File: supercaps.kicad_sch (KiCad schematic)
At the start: 17 parts, among them J8 XT30_F, J9 XT30_F, Q10 2SAR587D3, Q9 2SCR587D3, U17 TLV9301xDBV

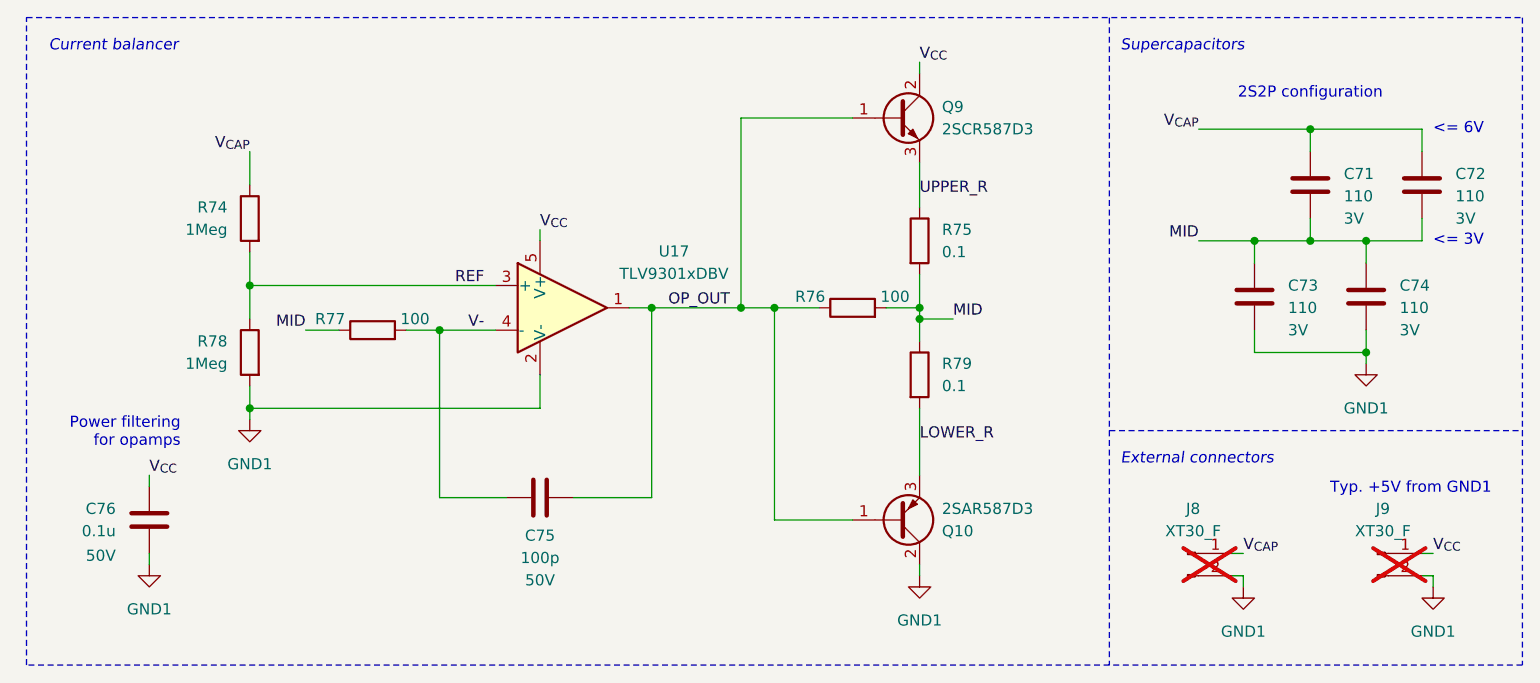
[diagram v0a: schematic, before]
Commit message: Add test points to all subsheets
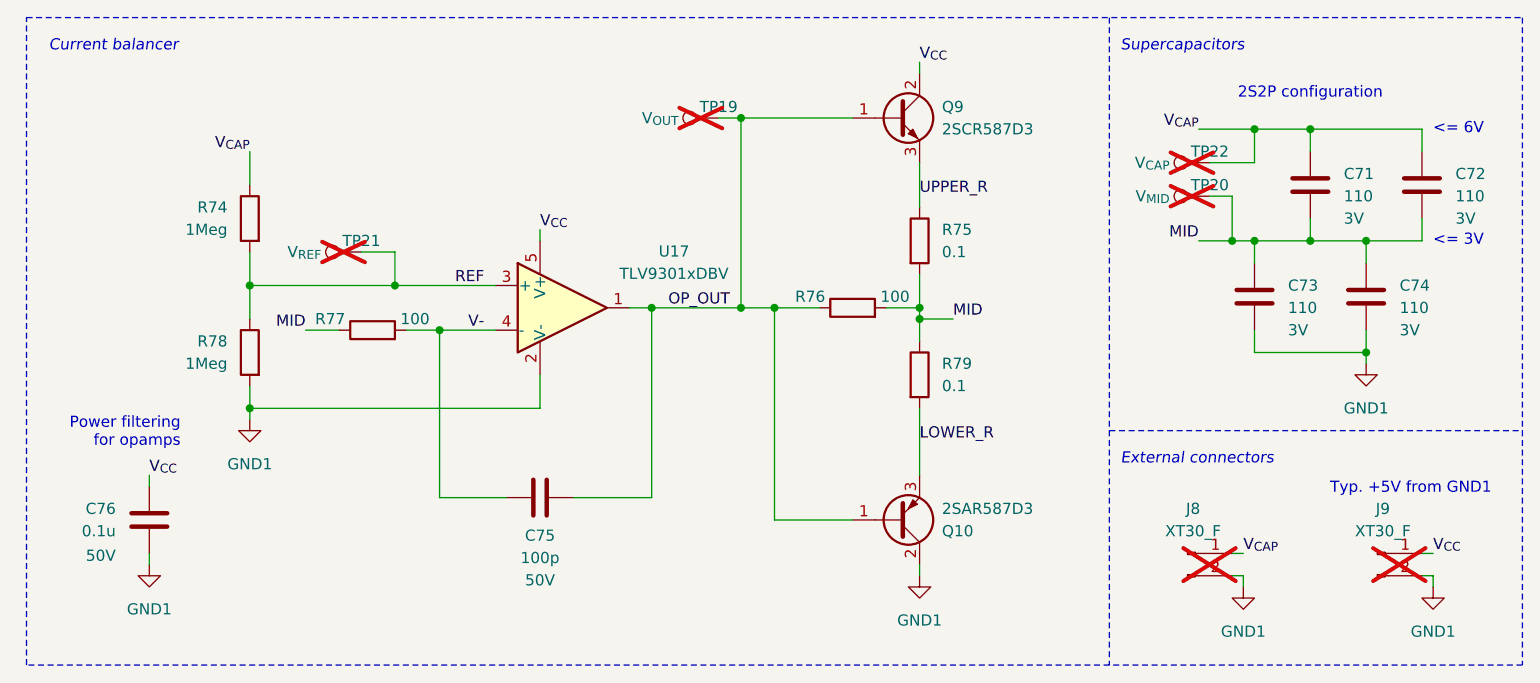
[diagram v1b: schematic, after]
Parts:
- added TP19: V_{OUT}, TestPoint:TestPoint_Bridge_Pitch2.0mm_Drill0.7mm, symbol Connector:TestPoint
- added TP20: V_{MID}, TestPoint:TestPoint_Bridge_Pitch2.0mm_Drill0.7mm, symbol Connector:TestPoint
- added TP21: V_{REF}, TestPoint:TestPoint_Bridge_Pitch2.0mm_Drill0.7mm, symbol Connector:TestPoint
- added TP22: V_{CAP}, TestPoint:TestPoint_Bridge_Pitch2.0mm_Drill0.7mm, symbol Connector:TestPoint
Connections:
- net MID: now also TP20.1
- net OP_OUT: now also TP19.1
- net REF: now also TP21.1
- net V_{CAP}: now also TP22.1

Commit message: Renumbered components for rev 1b layout
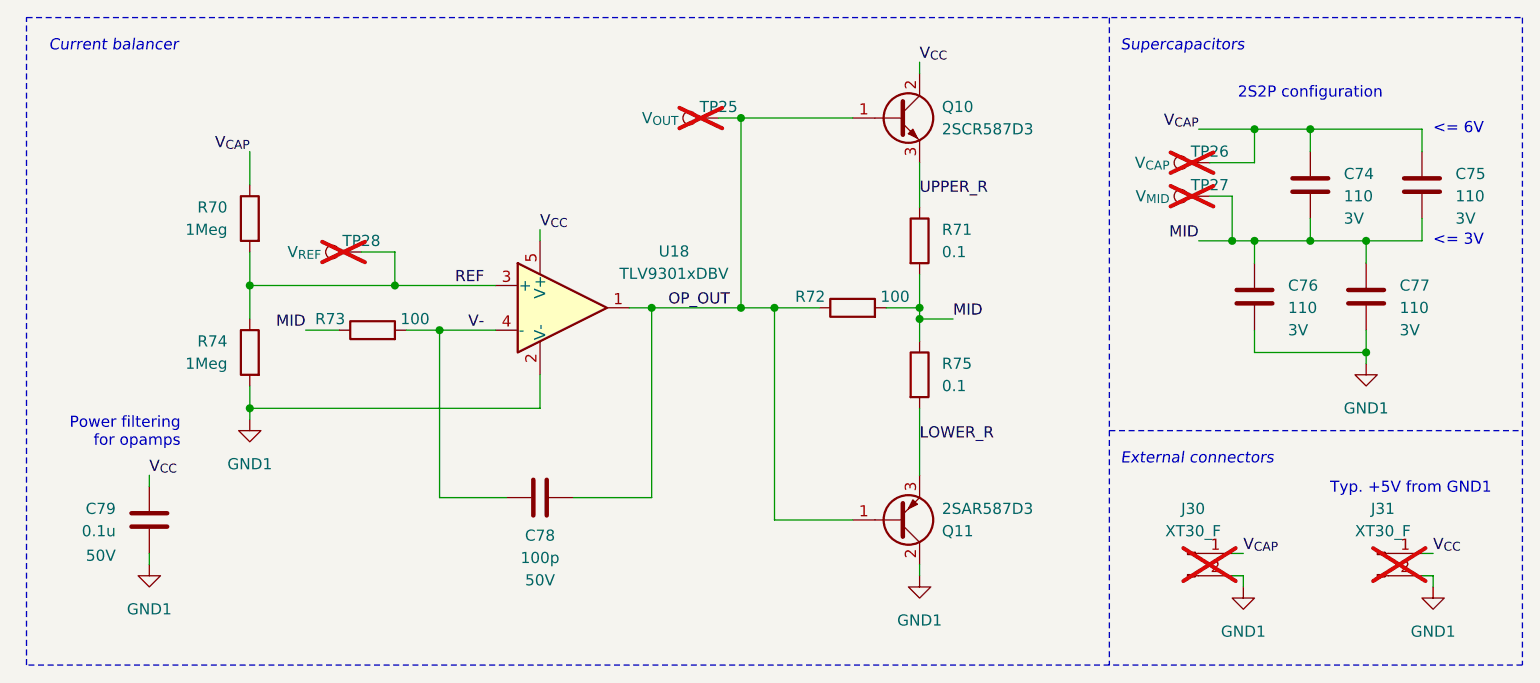
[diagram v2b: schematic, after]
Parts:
- renumbered C71 to C74, C72 to C75, C73 to C76, C74 to C77, C75 to C78, C76 to C79, J8 to J30, J9 to J31, Q9 to Q10, Q10 to Q11, R74 to R70, R75 to R71, R76 to R72, R77 to R73, R78 to R74, R79 to R75, TP19 to TP25, TP22 to TP26, TP20 to TP27, TP21 to TP28, U17 to U18
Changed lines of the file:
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@@
 		(on_board yes)
 		(dnp yes)
-		(property "Reference" "TP21"
+		(property "Reference" "TP28"
 			(at 59.69 50.8 90)
 			(effects
@@
 			(project "Rev 1B"
 				(path "/e5f99deb-ef42-4c5f-b80a-388477910e20/1165d5b5-e274-4083-890a-7a12aee56ddf"
-					(reference "TP21")
+					(reference "TP28")
 					(unit 1)
 				)
@@
 		(on_board yes)
 		(dnp no)
-		(property "Reference" "R?"
+		(property "Reference" "R75"
 			(at 125.73 64.7699 0)
 			(effects
@@
 			(project "Rev 1B"
 				(path "/e5f99deb-ef42-4c5f-b80a-388477910e20/1165d5b5-e274-4083-890a-7a12aee56ddf"
-					(reference "R?")
+					(reference "R75")
 					(unit 1)
 				)
@@
 		(on_board yes)
 		(dnp no)
-		(property "Reference" "U?"
+		(property "Reference" "U18"
 			(at 95.25 51.9998 0)
 			(effects
@@
 			(project "Rev 1B"
 				(path "/e5f99deb-ef42-4c5f-b80a-388477910e20/1165d5b5-e274-4083-890a-7a12aee56ddf"
-					(reference "U?")
+					(reference "U18")
 					(unit 1)
 				)
@@
 		(on_board yes)
 		(dnp yes)
-		(property "Reference" "TP19"
+		(property "Reference" "TP25"
 			(at 100.33 35.56 90)
 			(effects
@@
 			(project "Rev 1B"
 				(path "/e5f99deb-ef42-4c5f-b80a-388477910e20/1165d5b5-e274-4083-890a-7a12aee56ddf"
-					(reference "TP19")
+					(reference "TP25")
 					(unit 1)
 				)
@@
 		(on_board yes)
 		(dnp no)
-		(property "Reference" "C?"
+		(property "Reference" "C78"
 			(at 80.01 84.328 90)
 			(effects
@@
 			(project "Rev 1B"
 				(path "/e5f99deb-ef42-4c5f-b80a-388477910e20/1165d5b5-e274-4083-890a-7a12aee56ddf"
-					(reference "C?")
+					(reference "C78")
 					(unit 1)
 				)
@@
 		(on_board no)
 		(dnp no)
-		(property "Reference" "C?"
+		(property "Reference" "C76"
 			(at 165.1 55.8799 0)
 			(effects
@@
 			(project "Rev 1B"
 				(path "/e5f99deb-ef42-4c5f-b80a-388477910e20/1165d5b5-e274-4083-890a-7a12aee56ddf"
-					(reference "C?")
+					(reference "C76")
 					(unit 1)
 				)
@@
 		(dnp no)
 		(fields_autoplaced yes)
-		(property "Reference" "#PWR?"
+		(property "Reference" "#PWR0119"
 			(at 46.99 77.47 0)
 			(effects
@@
 			(project "Rev 1B"
 				(path "/e5f99deb-ef42-4c5f-b80a-388477910e20/1165d5b5-e274-4083-890a-7a12aee56ddf"
-					(reference "#PWR?")
+					(reference "#PWR0119")
 					(unit 1)
 				)
@@
 		(on_board yes)
 		(dnp no)
-		(property "Reference" "C?"
+		(property "Reference" "C79"
 			(at 31.75 81.2799 0)
 			(effects
@@
 			(project "Rev 1B"
 				(path "/e5f99deb-ef42-4c5f-b80a-388477910e20/1165d5b5-e274-4083-890a-7a12aee56ddf"
-					(reference "C?")
+					(reference "C79")
 					(unit 1)
 				)
@@
 		(dnp no)
 		(fields_autoplaced yes)
-		(property "Reference" "#PWR?"
+		(property "Reference" "#PWR0122"
 			(at 160.02 96.52 0)
 			(effects
@@
 			(project "Rev 1B"
 				(path "/e5f99deb-ef42-4c5f-b80a-388477910e20/1165d5b5-e274-4083-890a-7a12aee56ddf"
-					(reference "#PWR?")
+					(reference "#PWR0122")
 					(unit 1)
 				)
@@
 		(on_board yes)
 		(dnp yes)
-		(property "Reference" "J?"
+		(property "Reference" "J31"
 			(at 175.895 81.28 0)
 			(effects
@@
 			(project "Rev 1B"
 				(path "/e5f99deb-ef42-4c5f-b80a-388477910e20/1165d5b5-e274-4083-890a-7a12aee56ddf"
-					(reference "J?")
+					(reference "J31")
 					(unit 1)
 				)
@@
 		(dnp no)
 		(fields_autoplaced yes)
-		(property "Reference" "#PWR?"
+		(property "Reference" "#PWR0118"
 			(at 173.99 71.12 0)
 			(effects
@@
 			(project "Rev 1B"
 				(path "/e5f99deb-ef42-4c5f-b80a-388477910e20/1165d5b5-e274-4083-890a-7a12aee56ddf"
-					(reference "#PWR?")
+					(reference "#PWR0118")
 					(unit 1)
 				)
@@
 		(on_board yes)
 		(dnp yes)
-		(property "Reference" "TP22"
+		(property "Reference" "TP26"
 			(at 156.21 40.64 90)
 			(effects
@@
 			(project "Rev 1B"
 				(path "/e5f99deb-ef42-4c5f-b80a-388477910e20/1165d5b5-e274-4083-890a-7a12aee56ddf"
-					(reference "TP22")
+					(reference "TP26")
 					(unit 1)
 				)
@@
 		(on_board yes)
 		(dnp no)
-		(property "Reference" "R?"
+		(property "Reference" "R70"
 			(at 44.45 46.9899 0)
 			(effects
@@
 			(project "Rev 1B"
 				(path "/e5f99deb-ef42-4c5f-b80a-388477910e20/1165d5b5-e274-4083-890a-7a12aee56ddf"
-					(reference "R?")
+					(reference "R70")
 					(unit 1)
 				)
@@
 		(on_board no)
 		(dnp no)
-		(property "Reference" "C?"
+		(property "Reference" "C74"
 			(at 171.45 43.1799 0)
 			(effects
@@
 			(project "Rev 1B"
 				(path "/e5f99deb-ef42-4c5f-b80a-388477910e20/1165d5b5-e274-4083-890a-7a12aee56ddf"
-					(reference "C?")
+					(reference "C74")
 					(unit 1)
 				)
@@
 		(dnp no)
 		(fields_autoplaced yes)
-		(property "Reference" "#PWR?"
+		(property "Reference" "#PWR0121"
 			(at 123.19 95.25 0)
 			(effects
@@
 			(project "Rev 1B"
 				(path "/e5f99deb-ef42-4c5f-b80a-388477910e20/1165d5b5-e274-4083-890a-7a12aee56ddf"
-					(reference "#PWR?")
+					(reference "#PWR0121")
 					(unit 1)
 				)
@@
 		(on_board yes)
 		(dnp yes)
-		(property "Reference" "J?"
+		(property "Reference" "J30"
 			(at 154.305 81.28 0)
 			(effects
@@
 			(project "Rev 1B"
 				(path "/e5f99deb-ef42-4c5f-b80a-388477910e20/1165d5b5-e274-4083-890a-7a12aee56ddf"
-					(reference "J?")
+					(reference "J30")
 					(unit 1)
 				)
@@
 		(dnp no)
 		(fields_autoplaced yes)
-		(property "Reference" "Q?"
+		(property "Reference" "Q10"
 			(at 125.73 35.5599 0)
 			(effects
@@
 			(project "Rev 1B"
 				(path "/e5f99deb-ef42-4c5f-b80a-388477910e20/1165d5b5-e274-4083-890a-7a12aee56ddf"
-					(reference "Q?")
+					(reference "Q10")
 					(unit 1)
 				)
@@
 		(on_board yes)
 		(dnp yes)
-		(property "Reference" "TP20"
+		(property "Reference" "TP27"
 			(at 156.21 44.45 90)
 			(effects
@@
 			(project "Rev 1B"
 				(path "/e5f99deb-ef42-4c5f-b80a-388477910e20/1165d5b5-e274-4083-890a-7a12aee56ddf"
-					(reference "TP20")
+					(reference "TP27")
 					(unit 1)
 				)
@@
 		(on_board no)
 		(dnp no)
-		(property "Reference" "C?"
+		(property "Reference" "C75"
 			(at 184.15 43.1799 0)
 			(effects
@@
 			(project "Rev 1B"
 				(path "/e5f99deb-ef42-4c5f-b80a-388477910e20/1165d5b5-e274-4083-890a-7a12aee56ddf"
-					(reference "C?")
+					(reference "C75")
 					(unit 1)
 				)
@@
 		(on_board yes)
 		(dnp no)
-		(property "Reference" "R?"
+		(property "Reference" "R71"
 			(at 125.73 49.5299 0)
 			(effects
@@
 			(project "Rev 1B"
 				(path "/e5f99deb-ef42-4c5f-b80a-388477910e20/1165d5b5-e274-4083-890a-7a12aee56ddf"
-					(reference "R?")
+					(reference "R71")
 					(unit 1)
 				)
@@
 		(on_board yes)
 		(dnp no)
-		(property "Reference" "R?"
+		(property "Reference" "R74"
 			(at 44.45 62.2299 0)
 			(effects
@@
 			(project "Rev 1B"
 				(path "/e5f99deb-ef42-4c5f-b80a-388477910e20/1165d5b5-e274-4083-890a-7a12aee56ddf"
-					(reference "R?")
+					(reference "R74")
 					(unit 1)
 				)
@@
 		(on_board yes)
 		(dnp no)
-		(property "Reference" "R?"
+		(property "Reference" "R73"
 			(at 56.134 59.69 90)
 			(effects
@@
 			(project "Rev 1B"
 				(path "/e5f99deb-ef42-4c5f-b80a-388477910e20/1165d5b5-e274-4083-890a-7a12aee56ddf"
-					(reference "R?")
+					(reference "R73")
 					(unit 1)
 				)
@@
 		(dnp no)
 		(fields_autoplaced yes)
-		(property "Reference" "#PWR?"
+		(property "Reference" "#PWR0120"
 			(at 35.56 93.98 0)
 			(effects
@@
 			(project "Rev 1B"
 				(path "/e5f99deb-ef42-4c5f-b80a-388477910e20/1165d5b5-e274-4083-890a-7a12aee56ddf"
-					(reference "#PWR?")
+					(reference "#PWR0120")
 					(unit 1)
 				)
@@
 		(dnp no)
 		(fields_autoplaced yes)
-		(property "Reference" "#PWR?"
+		(property "Reference" "#PWR0123"
 			(at 181.61 96.52 0)
 			(effects
@@
 			(project "Rev 1B"
 				(path "/e5f99deb-ef42-4c5f-b80a-388477910e20/1165d5b5-e274-4083-890a-7a12aee56ddf"
-					(reference "#PWR?")
+					(reference "#PWR0123")
 					(unit 1)
 				)
@@
 		(on_board yes)
 		(dnp no)
-		(property "Reference" "R?"
+		(property "Reference" "R72"
 			(at 110.744 57.15 90)
 			(effects
@@
 			(project "Rev 1B"
 				(path "/e5f99deb-ef42-4c5f-b80a-388477910e20/1165d5b5-e274-4083-890a-7a12aee56ddf"
-					(reference "R?")
+					(reference "R72")
 					(unit 1)
 				)
@@
 		(on_board yes)
 		(dnp no)
-		(property "Reference" "Q?"
+		(property "Reference" "Q11"
 			(at 125.73 83.8201 0)
 			(effects
@@
 			(project "Rev 1B"
 				(path "/e5f99deb-ef42-4c5f-b80a-388477910e20/1165d5b5-e274-4083-890a-7a12aee56ddf"
-					(reference "Q?")
+					(reference "Q11")
 					(unit 1)
 				)
@@
 		(on_board no)
 		(dnp no)
-		(property "Reference" "C?"
+		(property "Reference" "C77"
 			(at 177.8 55.8799 0)
 			(effects
@@
 			(project "Rev 1B"
 				(path "/e5f99deb-ef42-4c5f-b80a-388477910e20/1165d5b5-e274-4083-890a-7a12aee56ddf"
-					(reference "C?")
-					(unit 1)
-				)
+					(reference "C77")
+					(unit 1)
+				)
